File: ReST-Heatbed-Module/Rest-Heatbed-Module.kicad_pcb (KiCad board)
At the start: 2 copper layers, 31 x 49.2 mm, 72 parts

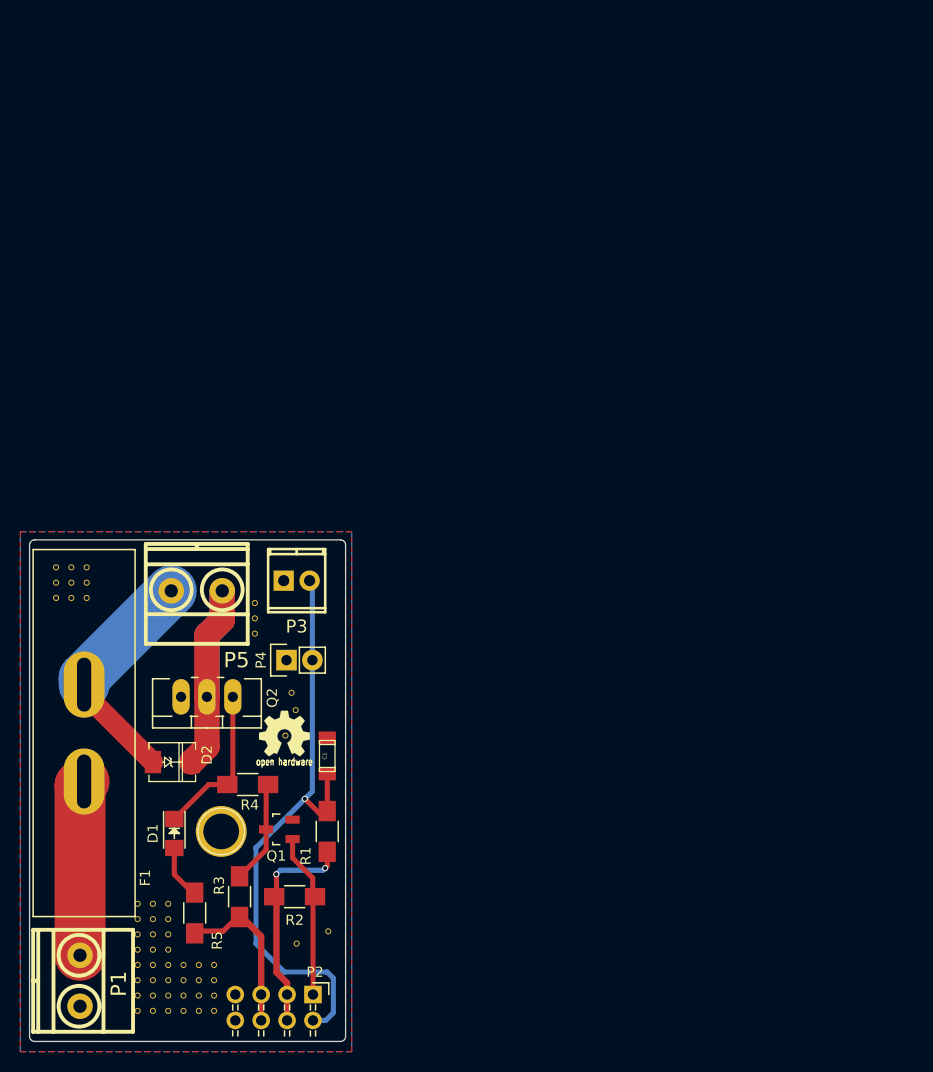
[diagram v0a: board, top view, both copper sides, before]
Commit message: Reworked Modules to sit ontop of the mainboard
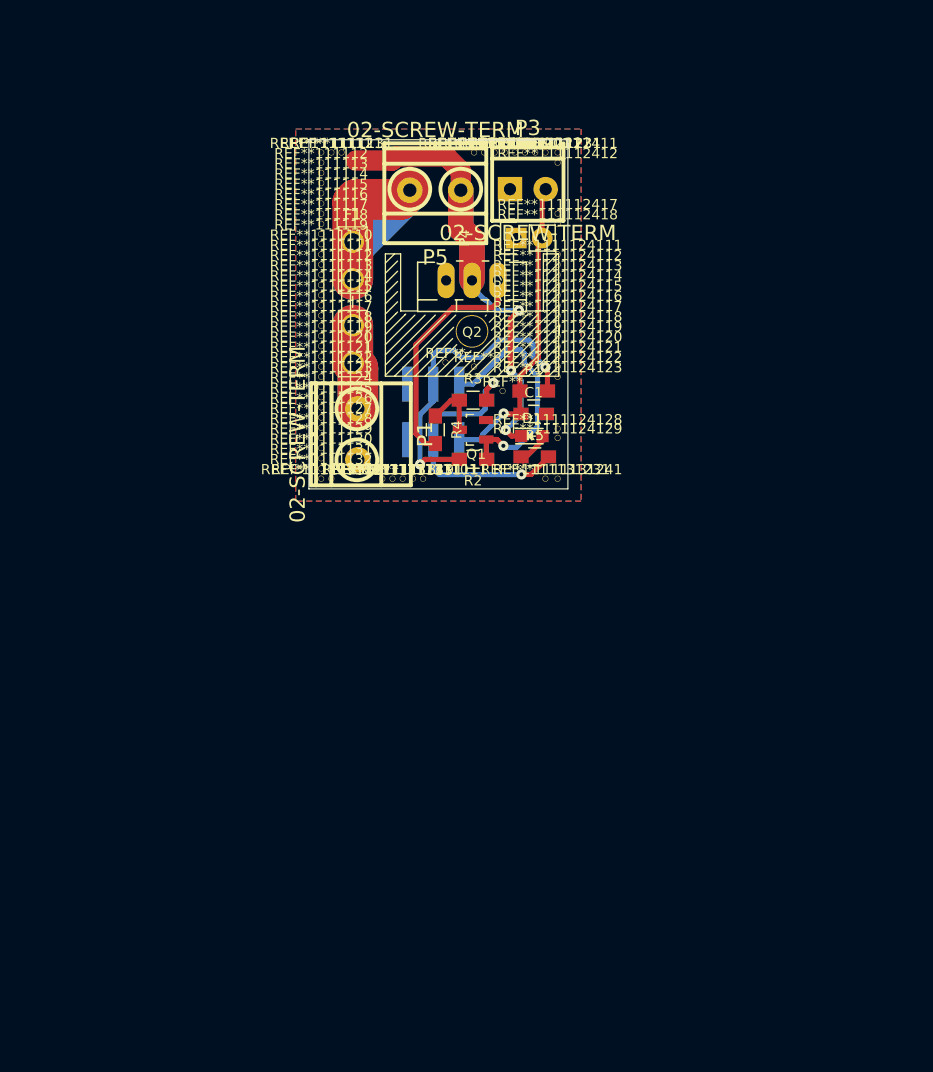
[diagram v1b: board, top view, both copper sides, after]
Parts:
- removed ? (x53): , ReST-Library:VIA-0.6mm
- removed ?: , ReST-Library:Logo_silk_OSHW_6x6mm
- removed ?: , ReST-Library:STM32
- removed ?: , Connect:1pin
- removed D2: , DO-214AC(SMA):DO-214AC(SMA)
- added REF**: 1pin, ReST-Library:1pin, F.Cu at (158.6, 90.8)
- added REF**: 1pin, ReST-Library:1pin, F.Cu at (155.8, 88.4)
- added REF**: 1pin, ReST-Library:1pin, F.Cu at (153.0, 88.0)
- added REF**1111110: 1pin, ReST-Library:1pin, F.Cu at (140.8, 76.4)
- added REF**1111111: 1pin, ReST-Library:1pin, F.Cu at (140.8, 77.4)
- added REF**1111111: 1pin, ReST-Library:1pin, F.Cu at (140.8, 67.4)
- added REF**1111112: 1pin, ReST-Library:1pin, F.Cu at (140.8, 78.4)
- added REF**1111113: 1pin, ReST-Library:1pin, F.Cu at (140.8, 79.4)
- added REF**1111114: 1pin, ReST-Library:1pin, F.Cu at (140.8, 80.4)
- added REF**1111115: 1pin, ReST-Library:1pin, F.Cu at (140.8, 81.4)
- added REF**1111116: 1pin, ReST-Library:1pin, F.Cu at (140.8, 82.4)
- added REF**1111117: 1pin, ReST-Library:1pin, F.Cu at (140.8, 83.4)
- added REF**11111171: 1pin, ReST-Library:1pin, F.Cu at (155.8, 67.4)
- added REF**11111171: 1pin, ReST-Library:1pin, F.Cu at (156.8, 67.4)
- added REF**1111118: 1pin, ReST-Library:1pin, F.Cu at (140.8, 84.4)
- added REF**11111181: 1pin, ReST-Library:1pin, F.Cu at (157.8, 67.4)
- added REF**1111119: 1pin, ReST-Library:1pin, F.Cu at (140.8, 85.4)
- added REF**11111191: 1pin, ReST-Library:1pin, F.Cu at (158.8, 67.4)
- added REF**111112: 1pin, ReST-Library:1pin, F.Cu at (140.8, 68.4)
- added REF**1111120: 1pin, ReST-Library:1pin, F.Cu at (140.8, 86.4)
- added REF**11111201: 1pin, ReST-Library:1pin, F.Cu at (159.8, 67.4)
- added REF**1111121: 1pin, ReST-Library:1pin, F.Cu at (141.8, 67.4)
- added REF**1111121: 1pin, ReST-Library:1pin, F.Cu at (140.8, 87.4)
- added REF**11111211: 1pin, ReST-Library:1pin, F.Cu at (160.8, 67.4)
- added REF**1111122: 1pin, ReST-Library:1pin, F.Cu at (140.8, 88.4)
- added REF**11111221: 1pin, ReST-Library:1pin, F.Cu at (161.8, 67.4)
- added REF**1111123: 1pin, ReST-Library:1pin, F.Cu at (140.8, 89.4)
- added REF**11111231: 1pin, ReST-Library:1pin, F.Cu at (162.8, 67.4)
- added REF**1111124: 1pin, ReST-Library:1pin, F.Cu at (140.8, 90.4)
- added REF**111112411: 1pin, ReST-Library:1pin, F.Cu at (164.0, 67.4)
- added REF**1111124111: 1pin, ReST-Library:1pin, F.Cu at (164.0, 77.4)
- added REF**1111124112: 1pin, ReST-Library:1pin, F.Cu at (164.0, 78.4)
- added REF**1111124113: 1pin, ReST-Library:1pin, F.Cu at (164.0, 79.4)
- added REF**1111124114: 1pin, ReST-Library:1pin, F.Cu at (164.0, 80.4)
- added REF**1111124115: 1pin, ReST-Library:1pin, F.Cu at (164.0, 81.4)
- added REF**1111124116: 1pin, ReST-Library:1pin, F.Cu at (164.0, 82.4)
- added REF**1111124117: 1pin, ReST-Library:1pin, F.Cu at (164.0, 83.4)
- added REF**1111124118: 1pin, ReST-Library:1pin, F.Cu at (164.0, 84.4)
- added REF**1111124119: 1pin, ReST-Library:1pin, F.Cu at (164.0, 85.4)
- added REF**111112412: 1pin, ReST-Library:1pin, F.Cu at (164.0, 68.4)
- added REF**1111124120: 1pin, ReST-Library:1pin, F.Cu at (164.0, 86.4)
- added REF**1111124121: 1pin, ReST-Library:1pin, F.Cu at (164.0, 87.4)
- added REF**1111124122: 1pin, ReST-Library:1pin, F.Cu at (164.0, 88.4)
- added REF**1111124123: 1pin, ReST-Library:1pin, F.Cu at (164.0, 89.4)
- added REF**1111124128: 1pin, ReST-Library:1pin, F.Cu at (164.0, 94.5)
- added REF**1111124129: 1pin, ReST-Library:1pin, F.Cu at (164.0, 95.4)
- added REF**111112417: 1pin, ReST-Library:1pin, F.Cu at (164.0, 73.4)
- added REF**111112418: 1pin, ReST-Library:1pin, F.Cu at (164.0, 74.4)
- added REF**1111125: 1pin, ReST-Library:1pin, F.Cu at (140.8, 91.4)
- added REF**1111126: 1pin, ReST-Library:1pin, F.Cu at (140.8, 92.4)
- added REF**1111127: 1pin, ReST-Library:1pin, F.Cu at (140.8, 93.4)
- added REF**1111128: 1pin, ReST-Library:1pin, F.Cu at (140.8, 94.4)
- added REF**1111129: 1pin, ReST-Library:1pin, F.Cu at (140.8, 95.4)
- added REF**111113: 1pin, ReST-Library:1pin, F.Cu at (140.8, 69.4)
- added REF**1111130: 1pin, ReST-Library:1pin, F.Cu at (140.8, 96.4)
- added REF**1111131: 1pin, ReST-Library:1pin, F.Cu at (142.8, 67.4)
- added REF**1111131: 1pin, ReST-Library:1pin, F.Cu at (140.8, 97.4)
- added REF**1111131101: 1pin, ReST-Library:1pin, F.Cu at (149.8, 99.4)
- added REF**111113111: 1pin, ReST-Library:1pin, F.Cu at (140.8, 99.4)
- added REF**1111131111: 1pin, ReST-Library:1pin, F.Cu at (150.8, 99.4)
- added REF**111113121: 1pin, ReST-Library:1pin, F.Cu at (141.8, 99.4)
- added REF**1111131231: 1pin, ReST-Library:1pin, F.Cu at (162.8, 99.4)
- added REF**1111131241: 1pin, ReST-Library:1pin, F.Cu at (164.0, 99.4)
- added REF**111113171: 1pin, ReST-Library:1pin, F.Cu at (146.8, 99.4)
- added REF**111113181: 1pin, ReST-Library:1pin, F.Cu at (147.8, 99.4)
- added REF**111113191: 1pin, ReST-Library:1pin, F.Cu at (148.8, 99.4)
- added REF**1111132: 1pin, ReST-Library:1pin, F.Cu at (140.8, 98.4)
- added REF**111114: 1pin, ReST-Library:1pin, F.Cu at (140.8, 70.4)
- added REF**111115: 1pin, ReST-Library:1pin, F.Cu at (140.8, 71.4)
- added REF**111116: 1pin, ReST-Library:1pin, F.Cu at (140.8, 72.4)
- added REF**111117: 1pin, ReST-Library:1pin, F.Cu at (140.8, 73.4)
- added REF**111118: 1pin, ReST-Library:1pin, F.Cu at (140.8, 74.4)
- added REF**111119: 1pin, ReST-Library:1pin, F.Cu at (140.8, 75.4)
- C1: value (none) -> 10uF; footprint ok-smd-generic:1206 -> Capacitors_SMD:C_0805_HandSoldering
- D1: value (none) -> LED; footprint LEDs:LED_1206 -> LEDs:LED_0805
- F1: value (none) -> 15A; footprint ReST-Librar:JEF-703C -> ReST-Library:MINI-FUSE
- P1, P5: value (none) -> 02-SCREW-TERM; footprint 5mm-pitch-terminal:mkds_1,5-2 -> ReST-Library:screw-5-2P
- P2: value (none) -> CONN_02X03; footprint ReST-Library:Pin_Header_Angled_2x04 -> ReST-Library:bb02-hp06; moved to B.Cu
- P3: value (none) -> 02-SCREW-TERM; footprint 2:mpt_0,5%2f2-2,54 -> ReST-Library:pt_1,5-2-3,5-h
- P4: value (none) -> 01X02-MALE
- Q1: value (none) -> Q_BSH105
- Q2: value (none) -> Q_AOT240L; footprint TO_SOT_Packages_THT:TO-220_Neutral123_Vertical_LargePads -> ReST-Library:TO-220_Neutral123_Vertical_LargePads_Heatsink
- R1: value (none) -> 4.7K; footprint Resistors_SMD:R_1206_HandSoldering -> Resistors_SMD:R_0805_HandSoldering
- R2, R3: value (none) -> 100K; footprint Resistors_SMD:R_1206_HandSoldering -> Resistors_SMD:R_0805_HandSoldering
- R4: value (none) -> 22R; footprint Resistors_SMD:R_1206_HandSoldering -> Resistors_SMD:R_0805_HandSoldering
- R5: value (none) -> 150R; footprint Resistors_SMD:R_1206_HandSoldering -> Resistors_SMD:R_0805_HandSoldering
- moved P1 60.1 mm to (144.4, 95.0)
- moved P2 58.4 mm to (151.8, 92.8), turned to 180 degrees
- moved R5 55.8 mm to (161.8, 97.3), turned to 0 degrees
- moved R3 53.8 mm to (155.7, 91.7), turned to 0 degrees
- moved D1 52.4 mm to (161.5, 95.2), turned to 0 degrees
- moved F1 49.8 mm to (143.9, 82.1)
- moved Q2 48.4 mm to (155.6, 80.0)
- moved R1 47.7 mm to (161.7, 90.8), turned to 0 degrees
- moved P4 47.1 mm to (159.9, 75.8)
- moved R2 46.3 mm to (155.7, 97.5)
- moved P5 45.7 mm to (152.0, 71.1)
- moved P3 45.2 mm to (161.1, 70.3)
- moved Q1 43.6 mm to (155.7, 94.6)
- moved R4 39.4 mm to (152.0, 94.6), turned to 270 degrees
- moved C1 39.2 mm to (161.7, 93.0), turned to 0 degrees
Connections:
- P2 pad 1: /PWM-HEATBED -> /T0
- P2 pad 2: /T0 -> /PWM-HEATBED
- P2 pad 3: +3V3 -> +5V
- P2 pad 5: +5V -> GND
- P2 pad 6: +5V -> GND
- P5 pad 1: Net-(D2-Pad2) -> Net-(D1-Pad1)
- Q2 pad 1: Net-(D1-Pad1) -> Net-(Q2-Pad1)
- Q2 pad 2: Net-(D2-Pad2) -> Net-(D1-Pad1)
- R4 pad 2: Net-(D1-Pad1) -> Net-(Q2-Pad1)
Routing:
- net Net-(D1-Pad1): track 15.4 -> 52.7 mm, vias 0 -> 3
- net /T0: track 60.0 -> 30.6 mm
- net Net-(D2-Pad2): track 29.1 -> 0.00 mm
- net Net-(Q2-Pad1): track 0.00 -> 22.9 mm
- net +5V: track 16.5 -> 27.9 mm, vias 0 -> 2
- net +3V3: track 21.8 -> 31.8 mm
- net /PWM-HEATBED: track 16.1 -> 23.8 mm, vias 0 -> 1
- net Net-(Q1-Pad3): track 10.2 -> 5.91 mm
- net Net-(D1-Pad2): track 5.43 -> 3.36 mm
- net +12V: track 23.1 -> 25.0 mm
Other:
- board size 31 x 49.2 mm -> 25.4 x 34.2 mm
- net class Default: clearance 0.2 -> 0.25; via_dia 0.6 -> 1
- rule trace_clearance: 0.2 -> 0.25
- rule trace_min: 0.2 -> 0.25
- rule via_min_size: 0.4 -> 0.8
- board text added: "2 ounce board!!"
- board text removed: "@maker_berry"
- board text removed: "ReST32 Heatbed Module Rev. A | Test"

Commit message: Mainboard structure made and most modules finished
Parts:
- removed REF** (x3), REF**1111110, REF**1111111 (x2), REF**1111112, REF**1111113, REF**1111114, REF**1111115, REF**1111116, REF**1111117, REF**11111171 (x2), REF**1111118, REF**11111181, REF**1111119, REF**11111191, REF**111112, REF**1111120, REF**11111201, REF**1111121 (x2), REF**11111211, REF**1111122, REF**11111221, REF**1111123, REF**11111231, REF**1111124, REF**111112411, REF**1111124111, REF**1111124112, REF**1111124113, REF**1111124114, REF**1111124115, REF**1111124116, REF**1111124117, REF**1111124118, REF**1111124119, REF**111112412, REF**1111124120, REF**1111124121, REF**1111124122, REF**1111124123, REF**1111124128, REF**1111124129, REF**111112417, REF**111112418, REF**1111125, REF**1111126, REF**1111127, REF**1111128, REF**1111129, REF**111113, REF**1111130, REF**1111131 (x2), REF**1111131101, REF**111113111, REF**1111131111, REF**111113121, REF**1111131231, REF**1111131241, REF**111113171, REF**111113181, REF**111113191, REF**1111132, REF**111114, REF**111115, REF**111116, REF**111117, REF**111118, REF**111119: 1pin, ReST-Library:1pin
- added ?: , ReST-Library:1pin, F.Cu at (180.7, 88.8)
- added ?: , ReST-Library:1pin, F.Cu at (177.5, 92.8)
- added ?: , ReST-Library:1pin, F.Cu at (176.4, 92.8)
- added ?: , ReST-Library:1pin, F.Cu at (175.3, 92.8)
- added ?: , ReST-Library:1pin, F.Cu at (174.2, 92.8)
- added ?: , ReST-Library:1pin, F.Cu at (173.0, 92.8)
- added ?: , ReST-Library:1pin, F.Cu at (171.9, 92.8)
- added ?: , ReST-Library:1pin, F.Cu at (170.8, 92.8)
- added ?: , ReST-Library:1pin, F.Cu at (169.7, 92.8)
- added ?: , ReST-Library:1pin, F.Cu at (196.4, 91.7)
- added ?: , ReST-Library:1pin, F.Cu at (196.4, 90.5)
- added ?: , ReST-Library:1pin, F.Cu at (196.4, 92.8)
- added ?: , ReST-Library:1pin, F.Cu at (196.4, 89.4)
- added ?: , ReST-Library:1pin, F.Cu at (196.4, 88.2)
- added ?: , ReST-Library:1pin, F.Cu at (196.4, 87.1)
- added ?: , ReST-Library:1pin, F.Cu at (196.4, 86.0)
- added ?: , ReST-Library:1pin, F.Cu at (196.4, 84.8)
- added ?: , ReST-Library:1pin, F.Cu at (196.4, 83.7)
- added ?: , ReST-Library:1pin, F.Cu at (196.4, 82.5)
- added ?: , ReST-Library:1pin, F.Cu at (196.4, 81.4)
- added ?: , ReST-Library:1pin, F.Cu at (196.4, 80.3)
- added ?: , ReST-Library:1pin, F.Cu at (196.4, 79.1)
- added ?: , ReST-Library:1pin, F.Cu at (195.3, 92.8)
- added ?: , ReST-Library:1pin, F.Cu at (196.4, 78.0)
- added ?: , ReST-Library:1pin, F.Cu at (196.4, 76.8)
- added ?: , ReST-Library:1pin, F.Cu at (196.4, 75.7)
- added ?: , ReST-Library:1pin, F.Cu at (196.4, 74.6)
- added ?: , ReST-Library:1pin, F.Cu at (196.4, 73.4)
- added ?: , ReST-Library:1pin, F.Cu at (196.4, 72.3)
- added ?: , ReST-Library:1pin, F.Cu at (196.4, 71.1)
- added ?: , ReST-Library:1pin, F.Cu at (196.4, 70.0)
- added ?: , ReST-Library:1pin, F.Cu at (196.4, 68.9)
- added ?: , ReST-Library:1pin, F.Cu at (196.4, 66.6)
- added ?: , ReST-Library:1pin, F.Cu at (194.2, 92.8)
- added ?: , ReST-Library:1pin, F.Cu at (196.4, 65.4)
- added ?: , ReST-Library:1pin, F.Cu at (196.4, 64.3)
- added ?: , ReST-Library:1pin, F.Cu at (196.4, 60.9)
- added ?: , ReST-Library:1pin, F.Cu at (196.4, 59.7)
- added ?: , ReST-Library:1pin, F.Cu at (168.6, 92.8)
- added ?: , ReST-Library:1pin, F.Cu at (168.6, 91.7)
- added ?: , ReST-Library:1pin, F.Cu at (168.6, 90.5)
- added ?: , ReST-Library:1pin, F.Cu at (168.6, 89.4)
- added ?: , ReST-Library:1pin, F.Cu at (168.6, 88.2)
- added ?: , ReST-Library:1pin, F.Cu at (168.6, 87.1)
- added ?: , ReST-Library:1pin, F.Cu at (183.1, 92.8)
- added ?: , ReST-Library:1pin, F.Cu at (168.6, 86.0)
- added ?: , ReST-Library:1pin, F.Cu at (168.6, 84.8)
- added ?: , ReST-Library:1pin, F.Cu at (168.6, 83.7)
- added ?: , ReST-Library:1pin, F.Cu at (168.6, 82.5)
- added ?: , ReST-Library:1pin, F.Cu at (168.6, 81.4)
- added ?: , ReST-Library:1pin, F.Cu at (168.6, 80.3)
- added ?: , ReST-Library:1pin, F.Cu at (168.6, 79.1)
- added ?: , ReST-Library:1pin, F.Cu at (168.6, 78.0)
- added ?: , ReST-Library:1pin, F.Cu at (168.6, 67.7)
- added ?: , ReST-Library:1pin, F.Cu at (168.6, 66.6)
- added ?: , ReST-Library:1pin, F.Cu at (181.9, 92.8)
- added ?: , ReST-Library:1pin, F.Cu at (196.4, 58.6)
- added ?: , ReST-Library:1pin, F.Cu at (195.3, 58.6)
- added ?: , ReST-Library:1pin, F.Cu at (194.2, 58.6)
- added ?: , ReST-Library:1pin, F.Cu at (193.1, 58.6)
- added ?: , ReST-Library:1pin, F.Cu at (192.0, 58.6)
- added ?: , ReST-Library:1pin, F.Cu at (190.8, 58.6)
- added ?: , ReST-Library:1pin, F.Cu at (189.7, 58.6)
- added ?: , ReST-Library:1pin, F.Cu at (188.6, 58.6)
- added ?: , ReST-Library:1pin, F.Cu at (187.5, 58.6)
- added ?: , ReST-Library:1pin, F.Cu at (177.5, 58.6)
- added ?: , ReST-Library:1pin, F.Cu at (180.8, 92.8)
- added ?: , ReST-Library:1pin, F.Cu at (176.4, 58.6)
- added ?: , ReST-Library:1pin, F.Cu at (175.3, 58.6)
- added ?: , ReST-Library:1pin, F.Cu at (174.2, 58.6)
- added ?: , ReST-Library:1pin, F.Cu at (173.0, 58.6)
- added ?: 1pin, ReST-Library:1pin, F.Cu at (182.6, 71.2)
- added ?: , ReST-Library:1pin, F.Cu at (168.6, 58.6)
- added ?: , ReST-Library:1pin, F.Cu at (179.7, 92.8)
- added ?: , ReST-Library:1pin, F.Cu at (178.6, 92.8)
- added D2: , ReST-Library:DO-214AC.SMA, F.Cu at (176.3, 62.4)
- added D3: , ReST-Library:DO-214AC.SMA, F.Cu at (176.3, 70.8)
- C1: value 10uF -> (none)
- D1: value LED -> (none)
- P1, P3, P5: value 02-SCREW-TERM -> (none)
- P2: value CONN_02X03 -> (none)
- P4: value 01X02-MALE -> (none)
- Q1: value Q_BSH105 -> (none)
- Q2: value Q_AOT240L -> (none)
- R1: value 4.7K -> (none)
- R2, R3: value 100K -> (none)
- R4: value 22R -> (none)
- R5: value 150R -> (none)
- moved C1 39.2 mm to (193.6, 70.3), turned to 180 degrees
- moved P2 37.7 mm to (189.2, 88.4)
- moved R1 36.6 mm to (193.4, 72.6), turned to 180 degrees
- moved P4 33.4 mm to (192.3, 67.6)
- moved P3 33.3 mm to (193.3, 62.1)
- moved P5 33.2 mm to (184.0, 62.4)
- moved R4 33.0 mm to (184.2, 87.4), turned to 0 degrees
- moved D1 32.9 mm to (193.4, 87.4)
- moved Q2 32.6 mm to (188.1, 76.6)
- moved R5 32.5 mm to (193.4, 90.0), turned to 180 degrees
- moved P1 32.2 mm to (172.8, 79.8)
- moved F1 31.1 mm to (171.1, 66.8)
- moved R3 28.5 mm to (184.2, 90.2)
- moved Q1 23.4 mm to (178.4, 88.8), turned to 180 degrees
- moved R2 20.9 mm to (174.6, 88.6), turned to 90 degrees
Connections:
- P2 pad 1: /T0 -> GND
- P2 pad 2: /PWM-HEATBED -> /T0
- P2 pad 3: +5V -> GND
- P2 pad 4: +3V3 -> /PWM-HEATBED
- P2 pad 5: GND -> +5V
- P2 pad 6: GND -> +3V3
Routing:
- net Net-(D1-Pad1): track 52.7 -> 87.6 mm, vias 3 -> 1
- net +5V: track 27.9 -> 11.5 mm, vias 2 -> 1
- net +12V: track 25.0 -> 34.5 mm
- net Net-(Q2-Pad1): track 22.9 -> 15.2 mm
- net /T0: track 30.6 -> 25.4 mm
- net /PWM-HEATBED: track 23.8 -> 19.3 mm
- net +3V3: track 31.8 -> 33.8 mm, vias 2 -> 3
- net Net-(Q1-Pad3): track 5.91 -> 7.29 mm
- net Net-(F1-Pad1): track 16.8 -> 17.9 mm
- net Net-(D1-Pad2): track 3.36 -> 2.72 mm
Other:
- board size 25.4 x 34.2 mm -> 29.8 x 36.2 mm
- net class Default: via_dia 1 -> 0.8
- rule via_min_size: 0.8 -> 0.6

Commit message: Save of work
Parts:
- removed the ? at (168.6, 80.3)
- removed the ? at (168.6, 79.1)
- removed the ? at (168.6, 78.0)
- removed the ? at (168.6, 67.7)
- removed the ? at (168.6, 66.6)
- removed the ? at (177.5, 58.6)
- removed the ? at (176.4, 58.6)
- removed the ? at (173.0, 58.6)
- added P6: CONN_02X02, ReST-Library:bb02-hp04, B.Cu at (190.8, 71.6)
- C1: value (none) -> 10uF
- D1: value (none) -> LED
- D3: value (none) -> D_Small
- P2: value (none) -> CONN_02X03
- P4: value (none) -> 01X02-MALE
- Q1: value (none) -> Q_BSH105/IRLML2502
- Q2: value (none) -> Q_AOT240L
- R1: value (none) -> 4.7K
- R2, R3: value (none) -> 100K
- R4: value (none) -> 22R
- R5: value (none) -> 150R
- moved ? 0.20 mm to (182.4, 71.2)
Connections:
- net Net-(D1-Pad1) renamed /MOSFET
- net Net-(F1-Pad1) renamed /12V-R
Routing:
- net /MOSFET: track 87.6 -> 29.4 mm
- net +12V: track 34.5 -> 0.00 mm
- net /12V-R: track 17.9 -> 0.00 mm
- added copper zone on B.Cu, net +12V
- added copper zone on F.Cu, net +12V
- added copper zone on B.Cu, net /12V-R
- added copper zone on F.Cu, net /12V-R
- added copper zone on B.Cu, net /MOSFET
- added copper zone on F.Cu, net /MOSFET

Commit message: minor changes
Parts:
- removed the ? at (188.6, 58.6)
- removed the ? at (187.5, 58.6)
- removed the ? at (174.2, 58.6)
- C1: value 10uF -> (none)
- D1: value LED -> (none)
- D3: value D_Small -> (none)
- F1: value 15A -> (none)
- P2: value CONN_02X03 -> (none)
- P4: value 01X02-MALE -> (none)
- P6: value CONN_02X02 -> (none)
- Q1: value Q_BSH105/IRLML2502 -> (none)
- Q2: value Q_AOT240L -> (none)
- R1: value 4.7K -> (none)
- R2, R3: value 100K -> (none)
- R4: value 22R -> (none)
- R5: value 150R -> (none)
- moved D2 1.15 mm to (176.3, 61.2)
- moved D3 0.79 mm to (177.1, 70.6)
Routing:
- net /MOSFET: track 29.4 -> 16.8 mm
